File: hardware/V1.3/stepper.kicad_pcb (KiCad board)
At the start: 4 copper layers, 40 x 40 mm, 119 parts, among them J101 USB-MINI-B-SMD, J102 DRILL, J103 DRILL, J104 DRILL, J105 DRILL, J401 STACK-UP-HIGH, J402 STACK-DOWN, J403 STACK-UP-HIGH, J404 STACK-DOWN, P201 black, P202 green, P301 CON-SENSOR, P302 CON-SENSOR, Q201 FDS8449, Q202 AO4421, Q203 2N7002, SW101 Reset, SW102 Erase, U101 AT91SAM3SXB, U102 82400152, U201 ZXCT1086, U202 TMC21XX, U501 LD1117, X101 16Mhz

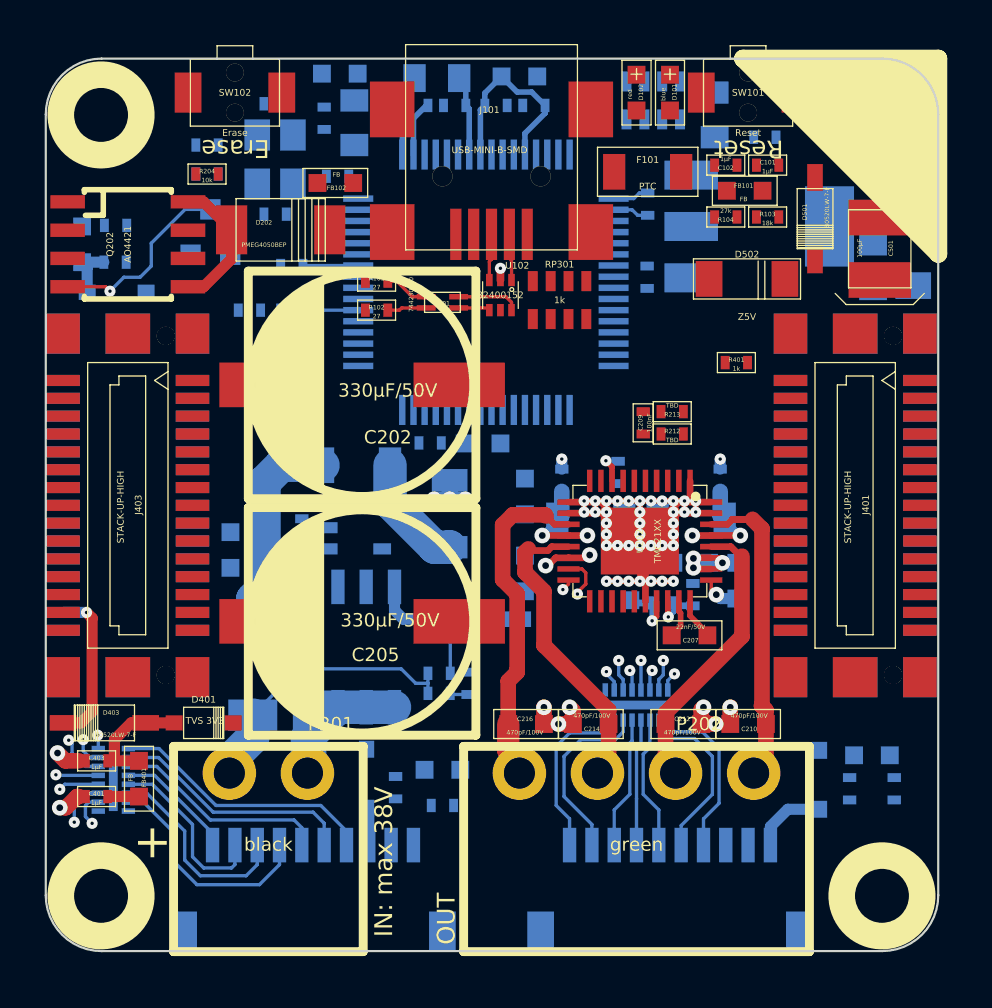
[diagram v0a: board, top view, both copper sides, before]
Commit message: change 0402, 0603 footprints to extended versions, fix placement
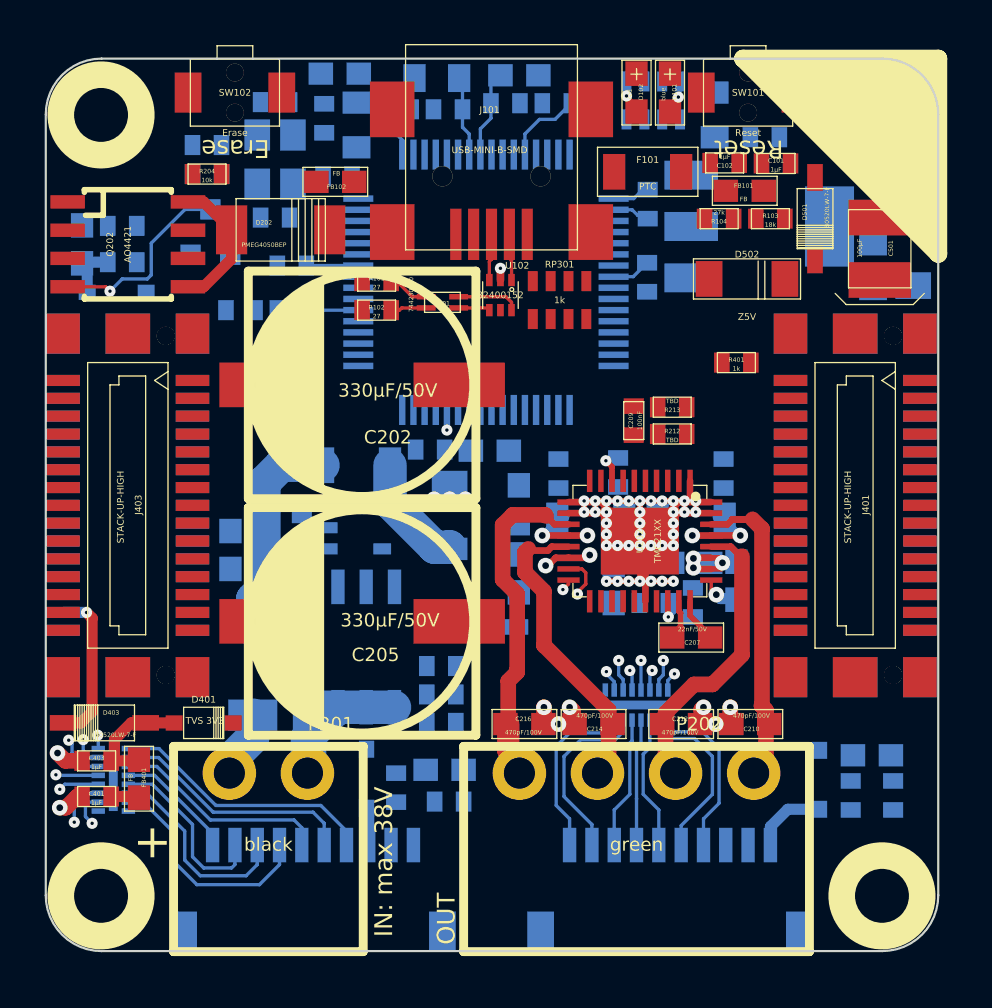
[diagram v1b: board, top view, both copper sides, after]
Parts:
- C101, C102, C103, C104, C201, C203, C209, C217, C218, C301, C302, C303, C304, C401, C402, C403, C404, C503, C506, C507, C508, C510, C511, C512, C513, C515, C517, C518, R101, R102, R103, R104, R202, R203, R204, R205, R206, R207, R208, R210, R211, R212, R213, R401, R501: footprint kicad-libraries:0402 -> kicad-libraries:0402E
- C204, C206, C207, C208, C210, C211, C212, C213, C214, C216, C505, C509, C516, FB101, FB102, FB301, FB302, FB401, FB402, R201: footprint kicad-libraries:0603 -> kicad-libraries:0603E
- D101, D102: footprint kicad-libraries:D0603 -> kicad-libraries:D0603E
- moved C510 2.73 mm to (149.6, 74.8), turned to 180 degrees
- moved R207 2.14 mm to (144.4, 102.5), turned to 180 degrees
- moved C511 1.28 mm to (147.3, 74.8), turned to 0 degrees
- moved C518 0.92 mm to (142.4, 75.0)
- moved C204 0.75 mm to (152.2, 96.3)
- moved C505 0.46 mm to (146.6, 90.3)
- moved C206 0.45 mm to (147.9, 92.8)
- moved C209 0.44 mm to (153.1, 89.0)
- moved R211 0.43 mm to (154.0, 97.2)
- moved R208 0.40 mm to (135.4, 84.0)
- moved C101 0.38 mm to (159.4, 77.5)
- moved D201 0.37 mm to (145.9, 98.2)
- moved C203 0.35 mm to (155.7, 97.2)
- moved C302 0.35 mm to (144.8, 106.1)
- moved C503 0.35 mm to (144.8, 75.0)
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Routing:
- net Net-(D203-Pad1): track 12.9 -> 3.04 mm
- net Net-(D201-Pad2): track 5.74 -> 0.00 mm
- net GND: track 8.06 -> 5.23 mm, vias 2 -> 4
- net Net-(C204-Pad1): track 2.79 -> 0.00 mm, vias 1 -> 0
- net (no net): track 2.15 -> 0.00 mm, vias 2 -> 0
- net Net-(D102-Pad2): track 0.00 -> 1.49 mm, vias 0 -> 1
- net Net-(D101-Pad2): track 0.00 -> 1.49 mm, vias 0 -> 1
- net Net-(C203-Pad1): track 2.33 -> 1.10 mm
- net Net-(C218-Pad2): track 4.51 -> 3.41 mm
- net Net-(C217-Pad2): track 4.36 -> 3.26 mm
- net PWR-SCK_CFG2: track 0.00 -> 0.90 mm, vias 0 -> 1
- net STACK-PGND: track 61.6 -> 60.7 mm, vias 49 -> 47
- net PWR-VEXT: track 0.82 -> 0.07 mm

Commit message: fix placement, no drc errors
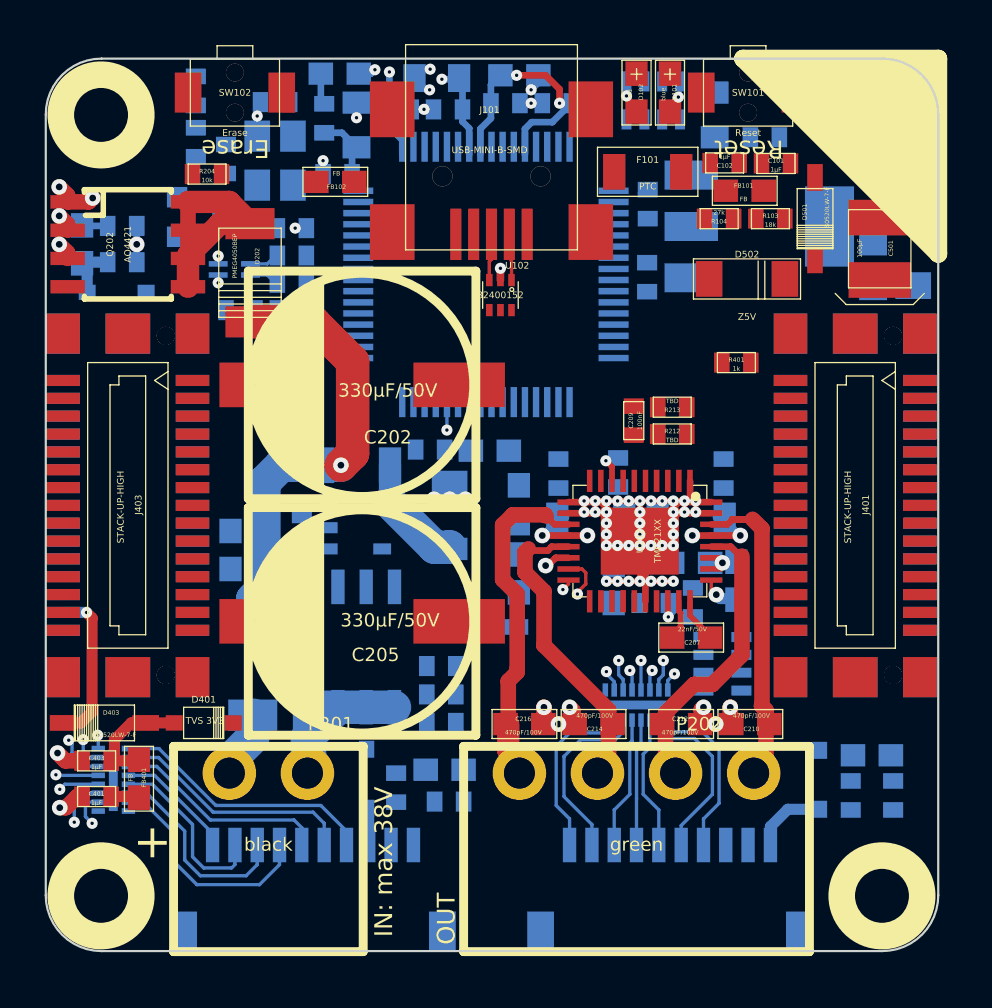
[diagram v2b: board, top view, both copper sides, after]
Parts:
- L101, R101, R102, RP301: moved to B.Cu
- moved RP301 17.9 mm to (157.1, 99.9), turned to 90 degrees
- moved L101 9.44 mm to (135.2, 82.2)
- moved R102 4.52 mm to (137.8, 81.6), turned to 0 degrees
- moved R101 3.80 mm to (137.8, 82.8), turned to 0 degrees
- moved R203 3.76 mm to (133.4, 74.2), turned to 90 degrees
- moved C103 3.42 mm to (134.8, 77.3), turned to 90 degrees
- moved D202 2.37 mm to (135.9, 82.4), turned to 90 degrees
- moved C508 1.67 mm to (137.8, 80.4)
- moved Q203 0.83 mm to (133.6, 79.9), turned to 270 degrees
- moved R202 0.52 mm to (133.4, 76.5), turned to 90 degrees
- moved U101 0.35 mm to (146.4, 82.5)
- moved C517 0.10 mm to (139.8, 78.0)
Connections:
- R101 pad 1: Net-(L101-Pad3) -> Net-(L101-Pad4)
- R102 pad 1: Net-(L101-Pad2) -> Net-(L101-Pad1)
- RP301 pad 5: BRICKLET-I2C-SCL -> BRICKLET-I2C-SDA
- RP301 pad 8: BRICKLET-I2C-SDA -> BRICKLET-I2C-SCL
- U102 pad 4: Net-(L101-Pad1) -> Net-(L101-Pad2)
- U102 pad 6: Net-(L101-Pad4) -> Net-(L101-Pad3)
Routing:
- net Net-(D202-Pad2): track 9.25 -> 20.3 mm, vias 0 -> 1
- net GND: track 5.23 -> 14.9 mm, vias 4 -> 13
- net VEE: track 24.0 -> 15.1 mm, vias 5 -> 2
- net Net-(Q202-PadG): track 8.83 -> 0.00 mm, vias 1 -> 0
- net Net-(D202-Pad1): track 6.24 -> 11.8 mm
- net STACK-PVCC: track 0.00 -> 3.61 mm, vias 0 -> 4
- net Net-(C517-Pad1): track 0.00 -> 3.10 mm
- net Net-(L101-Pad3): track 2.01 -> 0.35 mm, vias 0 -> 1
- net Net-(L101-Pad2): track 1.77 -> 0.35 mm, vias 0 -> 1
- net Net-(C516-Pad1): track 0.00 -> 1.41 mm
- net Net-(L101-Pad4): track 2.75 -> 1.34 mm
- net VSTACK: track 0.00 -> 1.16 mm
- net 3V3: track 14.9 -> 13.9 mm, vias 2 -> 5
- net Net-(C509-Pad1): track 11.7 -> 12.4 mm, vias 0 -> 3

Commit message: add power routing
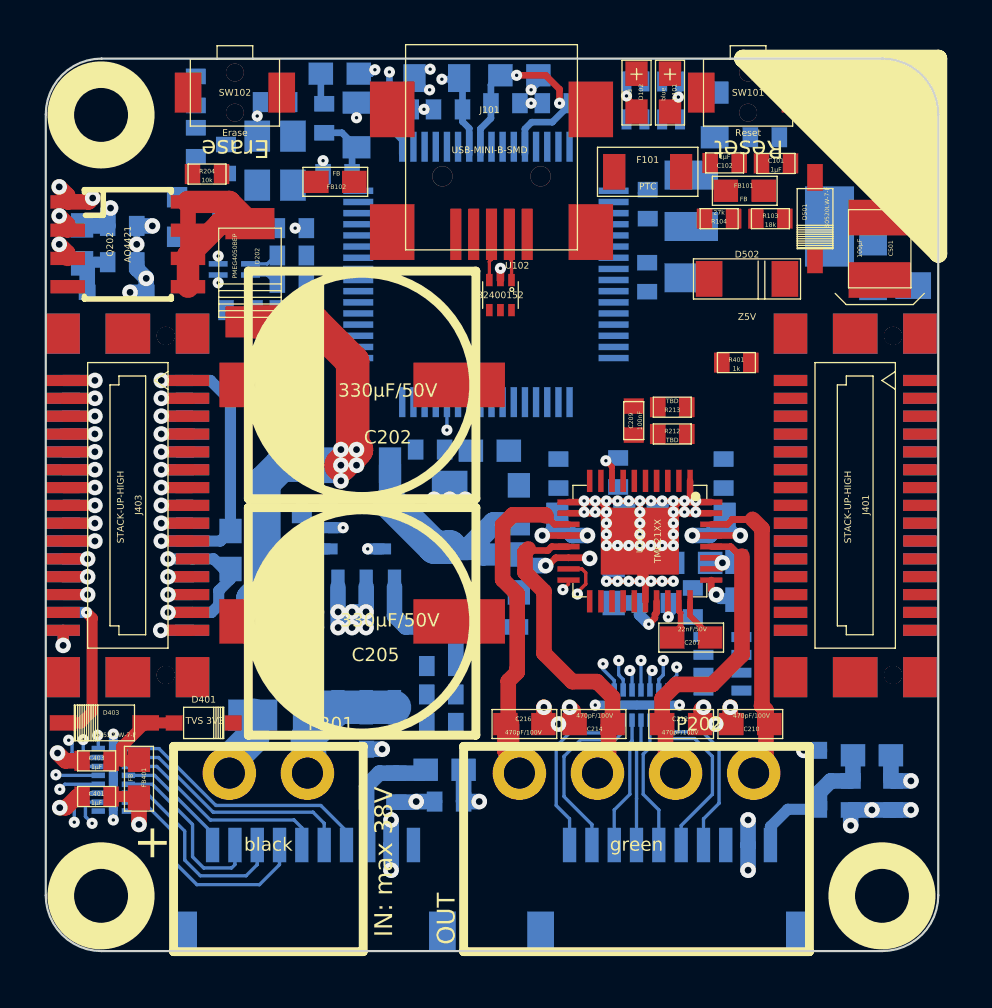
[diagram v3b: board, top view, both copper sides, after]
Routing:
- net STACK-PGND: track 60.7 -> 105.4 mm, vias 47 -> 65
- net GND: track 14.9 -> 49.9 mm, vias 13 -> 35
- net STACK-PVCC: track 3.61 -> 32.1 mm, vias 4 -> 14
- net VEE: track 15.1 -> 26.5 mm, vias 2 -> 3
- net Net-(C404-Pad1): track 2.42 -> 9.01 mm, vias 0 -> 3
- net Net-(D201-Pad2): track 0.00 -> 5.78 mm
- net Net-(D202-Pad2): track 20.3 -> 25.7 mm, vias 1 -> 5
- net 3V3: track 13.9 -> 17.8 mm, vias 5 -> 8
- net Net-(C304-Pad1): track 1.70 -> 5.64 mm
- net Net-(C303-Pad1): track 3.35 -> 6.92 mm
- net Net-(C204-Pad1): track 0.00 -> 3.45 mm, vias 0 -> 1
- net Net-(J403-Pad29): track 0.00 -> 2.85 mm, vias 0 -> 1
- net VSTACK: track 1.16 -> 4.00 mm, vias 0 -> 2
- net Net-(C218-Pad2): track 3.41 -> 4.86 mm
- net Net-(J403-Pad30): track 0.00 -> 1.36 mm, vias 0 -> 1
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
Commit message: more power routing
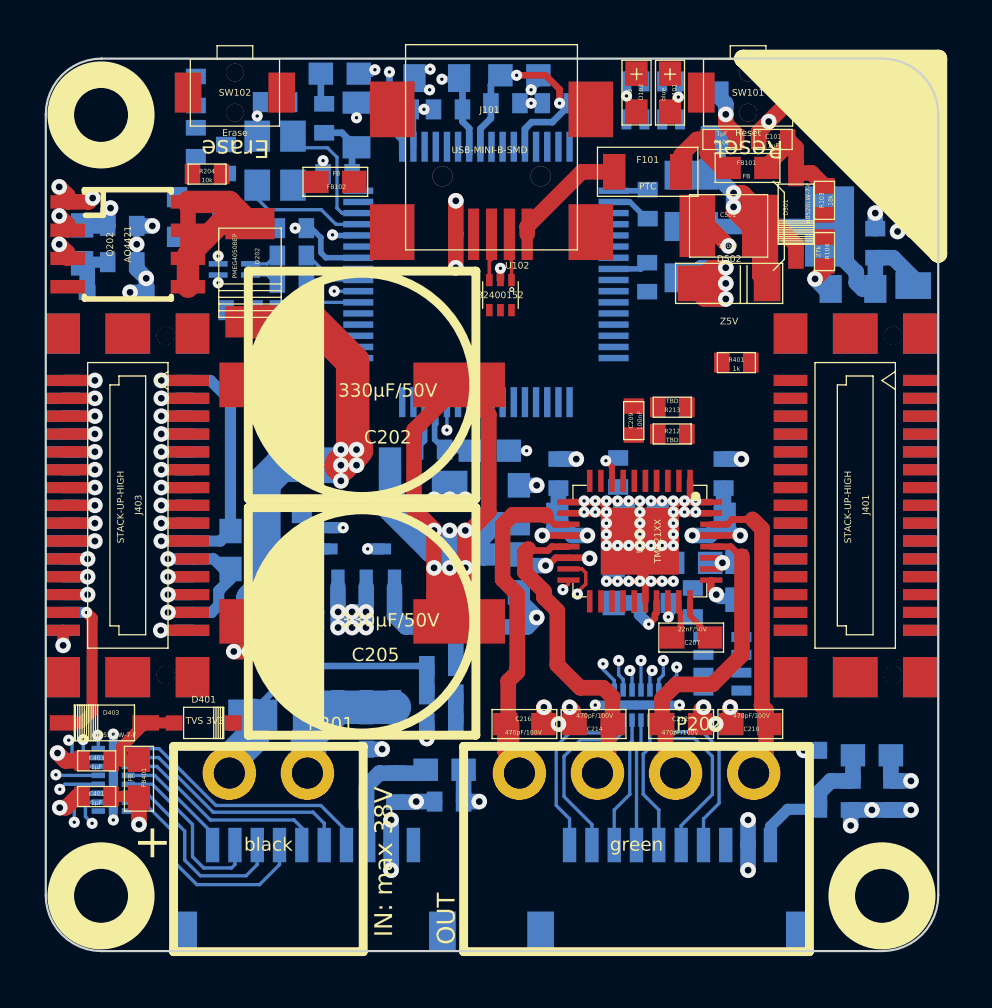
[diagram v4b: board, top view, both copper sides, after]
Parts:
- moved C515 6.86 mm to (163.9, 81.0), turned to 90 degrees
- moved C501 6.85 mm to (157.3, 80.3), turned to 180 degrees
- moved R104 4.95 mm to (161.6, 81.4), turned to 90 degrees
- moved R103 2.56 mm to (161.6, 79.1), turned to 270 degrees
- moved C514 1.35 mm to (162.9, 83.1), turned to 180 degrees
- moved C101 1.08 mm to (159.3, 76.4)
- moved C102 1.06 mm to (157.0, 76.4)
- moved FB101 1.03 mm to (158.2, 77.7)
- moved D501 0.87 mm to (160.3, 79.8)
- moved D502 0.82 mm to (157.3, 82.8)
- turned D503 to 90 degrees
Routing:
- net GND: track 49.9 -> 84.6 mm, vias 35 -> 51
- net VEE: track 26.5 -> 58.5 mm, vias 3 -> 9
- net 3V3: track 17.8 -> 40.5 mm
- net VSTACK: track 4.00 -> 20.9 mm, vias 2 -> 4
- net STACK-PGND: track 105.4 -> 117.2 mm, vias 65 -> 77
- net Net-(D203-Pad1): track 3.04 -> 13.1 mm
- net XIN: track 0.00 -> 5.69 mm
- net XOUT: track 0.00 -> 5.60 mm
- net Net-(F101-Pad2): track 0.00 -> 5.26 mm
- net VUSB: track 0.00 -> 4.84 mm
- net Net-(C509-Pad1): track 12.4 -> 16.5 mm
- net Net-(C102-Pad1): track 0.00 -> 4.06 mm
- net Net-(R102-Pad2): track 0.10 -> 2.68 mm
- net Net-(R101-Pad2): track 0.32 -> 2.70 mm
- net Net-(C218-Pad2): track 4.86 -> 6.33 mm
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
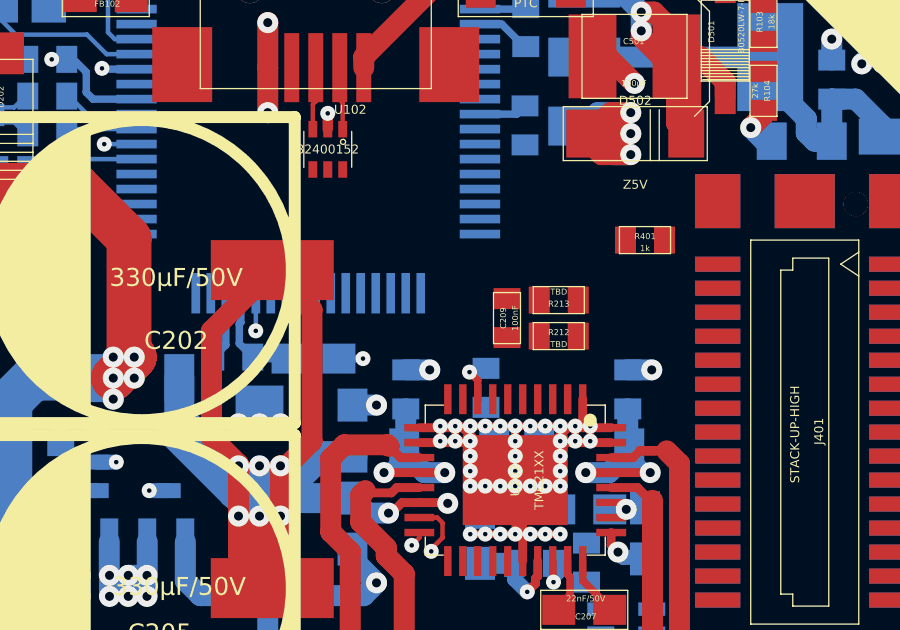
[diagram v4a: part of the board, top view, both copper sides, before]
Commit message: routing improved
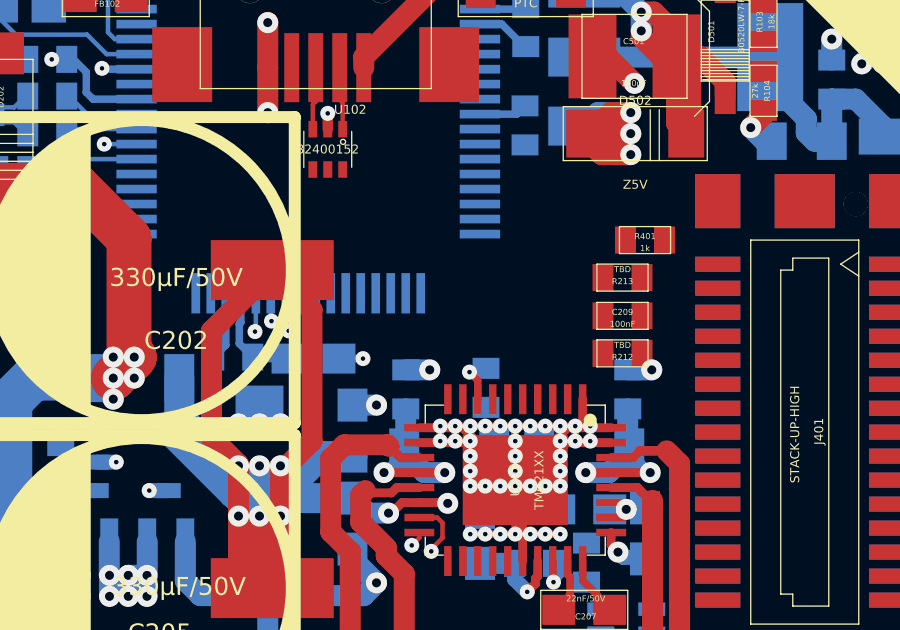
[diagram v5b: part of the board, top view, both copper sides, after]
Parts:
- moved C209 3.85 mm to (156.9, 88.9), turned to 180 degrees
- moved R213 2.25 mm to (156.9, 87.7)
- moved R212 2.20 mm to (156.9, 90.2), turned to 0 degrees
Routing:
- net PWR-DIAG1: track 0.00 -> 1.29 mm, vias 0 -> 1
- net BRICKLET-I2C-SDA: track 2.71 -> 3.64 mm, vias 2 -> 3
